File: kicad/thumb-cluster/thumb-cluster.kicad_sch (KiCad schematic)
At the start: 15 parts, among them J4 59453-081110EDHLF

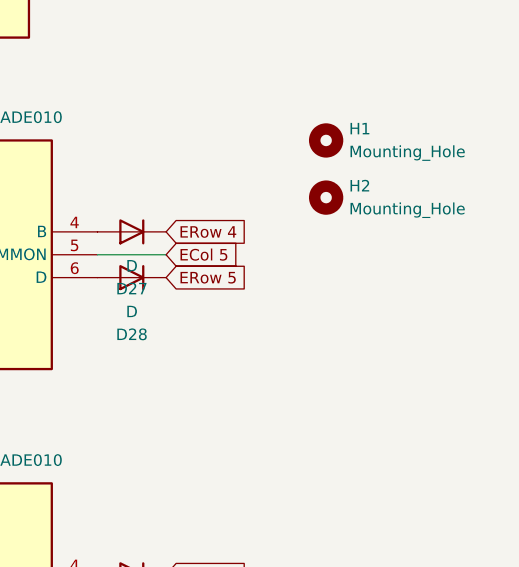
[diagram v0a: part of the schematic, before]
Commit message: update thumb cluster
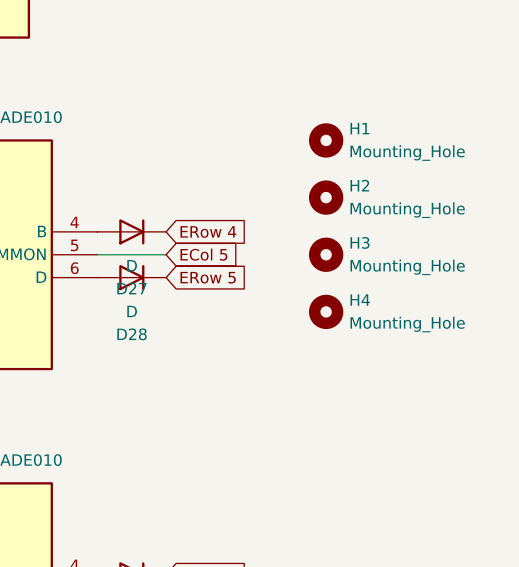
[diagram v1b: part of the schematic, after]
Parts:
- added H3, H4: Mounting_Hole, footprints:MountingHole_2.2mm_M2_Pad_Via, symbol ScottoKeebs:Placeholder_Mounting_Hole
- H1, H2: footprint MountingHole:MountingHole_2.2mm_M2_Pad_Via -> footprints:MountingHole_2.2mm_M2_Pad_Via
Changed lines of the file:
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@@
 			)
 		)
-		(property "Footprint" "MountingHole:MountingHole_2.2mm_M2_Pad_Via"
+		(property "Footprint" "footprints:MountingHole_2.2mm_M2_Pad_Via"
 			(at 115.57 67.31 0)
 			(effects
@@
 	)
 	(symbol
+		(lib_id "ScottoKeebs:Placeholder_Mounting_Hole")
+		(at 115.57 86.36 0)
+		(unit 1)
+		(exclude_from_sim no)
+		(in_bom yes)
+		(on_board yes)
+		(dnp no)
+		(fields_autoplaced yes)
+		(property "Reference" "H4"
+			(at 118.11 85.0899 0)
+			(effects
+				(font
+					(size 1.27 1.27)
+				)
+				(justify left)
+			)
+		)
+		(property "Value" "Mounting_Hole"
+			(at 118.11 87.6299 0)
+			(effects
+				(font
+					(size 1.27 1.27)
+				)
+				(justify left)
+			)
+		)
+		(property "Footprint" "footprints:MountingHole_2.2mm_M2_Pad_Via"
+			(at 115.57 86.36 0)
+			(effects
+				(font
+					(size 1.27 1.27)
+				)
+				(hide yes)
+			)
+		)
+		(property "Datasheet" "~"
+			(at 115.57 86.36 0)
+			(effects
+				(font
+					(size 1.27 1.27)
+				)
+				(hide yes)
+			)
+		)
+		(property "Description" "Mounting Hole without connection"
+			(at 115.57 86.36 0)
+			(effects
+				(font
+					(size 1.27 1.27)
+				)
+				(hide yes)
+			)
+		)
+		(instances
+			(project "thumb-cluster"
+				(path "/feb70c3f-3e34-4f8f-9694-07d231f2d237"
+					(reference "H4")
+					(unit 1)
+				)
+			)
+		)
+	)
+	(symbol
 		(lib_id "Device:D")
 		(at 50.8 115.57 0)
@@
 	)
 	(symbol
+		(lib_id "ScottoKeebs:Placeholder_Mounting_Hole")
+		(at 115.57 80.01 0)
+		(unit 1)
+		(exclude_from_sim no)
+		(in_bom yes)
+		(on_board yes)
+		(dnp no)
+		(fields_autoplaced yes)
+		(property "Reference" "H3"
+			(at 118.11 78.7399 0)
+			(effects
+				(font
+					(size 1.27 1.27)
+				)
+				(justify left)
+			)
+		)
+		(property "Value" "Mounting_Hole"
+			(at 118.11 81.2799 0)
+			(effects
+				(font
+					(size 1.27 1.27)
+				)
+				(justify left)
+			)
+		)
+		(property "Footprint" "footprints:MountingHole_2.2mm_M2_Pad_Via"
+			(at 115.57 80.01 0)
+			(effects
+				(font
+					(size 1.27 1.27)
+				)
+				(hide yes)
+			)
+		)
+		(property "Datasheet" "~"
+			(at 115.57 80.01 0)
+			(effects
+				(font
+					(size 1.27 1.27)
+				)
+				(hide yes)
+			)
+		)
+		(property "Description" "Mounting Hole without connection"
+			(at 115.57 80.01 0)
+			(effects
+				(font
+					(size 1.27 1.27)
+				)
+				(hide yes)
+			)
+		)
+		(instances
+			(project "thumb-cluster"
+				(path "/feb70c3f-3e34-4f8f-9694-07d231f2d237"
+					(reference "H3")
+					(unit 1)
+				)
+			)
+		)
+	)
+	(symbol
 		(lib_id "Device:D")
 		(at 50.8 82.55 0)
@@
 			)
 		)
-		(property "Footprint" "MountingHole:MountingHole_2.2mm_M2_Pad_Via"
+		(property "Footprint" "footprints:MountingHole_2.2mm_M2_Pad_Via"
 			(at 115.57 73.66 0)
 			(effects
